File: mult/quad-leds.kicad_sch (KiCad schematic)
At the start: 14 parts, among them U5 LM324

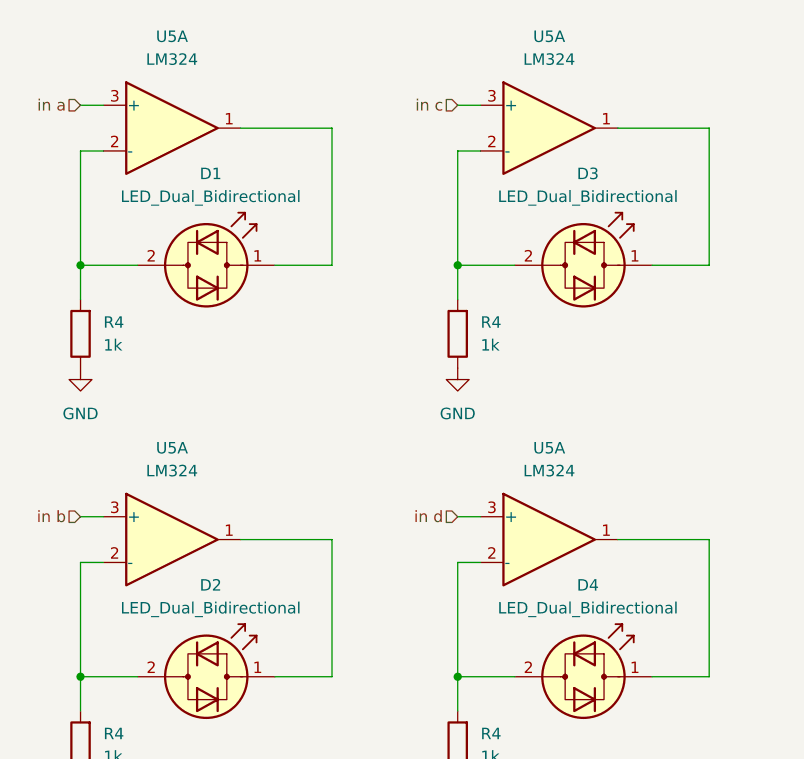
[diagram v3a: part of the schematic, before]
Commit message: mult: Manually assign references, grouped by value
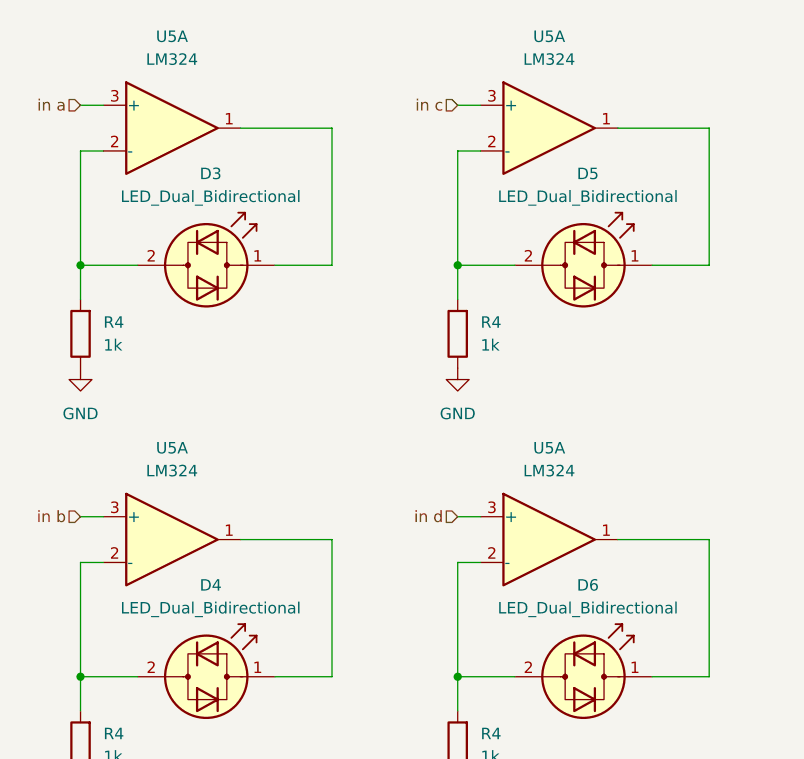
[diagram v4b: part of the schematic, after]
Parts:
- renumbered D1 to D3, D2 to D4, D3 to D5, D4 to D6
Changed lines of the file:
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@@
         )
         (path "/0e98ec4b-b4c7-447c-abd7-a761177a7f67/41fcec89-2c3a-419b-9d1d-2962d3c6916c"
-          (reference "C10") (unit 1)
+          (reference "C12") (unit 1)
         )
       )
@@
   (symbol (lib_id "Device:LED_Dual_Bidirectional") (at 135.89 148.59 0) (unit 1)
     (in_bom yes) (on_board yes) (dnp no) (fields_autoplaced)
-    (property "Reference" "D4" (at 136.3853 138.43 0)
+    (property "Reference" "D6" (at 136.3853 138.43 0)
       (effects (font (size 1.27 1.27)))
     )
@@
       (project "mult"
         (path "/0e98ec4b-b4c7-447c-abd7-a761177a7f67/41fcec89-2c3a-419b-9d1d-2962d3c6916c"
-          (reference "D4") (unit 1)
+          (reference "D6") (unit 1)
         )
       )
@@
   (symbol (lib_id "Device:LED_Dual_Bidirectional") (at 135.89 102.87 0) (unit 1)
     (in_bom yes) (on_board yes) (dnp no) (fields_autoplaced)
-    (property "Reference" "D3" (at 136.3853 92.71 0)
+    (property "Reference" "D5" (at 136.3853 92.71 0)
       (effects (font (size 1.27 1.27)))
     )
@@
       (project "mult"
         (path "/0e98ec4b-b4c7-447c-abd7-a761177a7f67/41fcec89-2c3a-419b-9d1d-2962d3c6916c"
-          (reference "D3") (unit 1)
+          (reference "D5") (unit 1)
         )
       )
@@
   (symbol (lib_id "Device:LED_Dual_Bidirectional") (at 93.98 102.87 0) (unit 1)
     (in_bom yes) (on_board yes) (dnp no) (fields_autoplaced)
-    (property "Reference" "D1" (at 94.4753 92.71 0)
+    (property "Reference" "D3" (at 94.4753 92.71 0)
       (effects (font (size 1.27 1.27)))
     )
@@
       (project "mult"
         (path "/0e98ec4b-b4c7-447c-abd7-a761177a7f67/41fcec89-2c3a-419b-9d1d-2962d3c6916c"
-          (reference "D1") (unit 1)
+          (reference "D3") (unit 1)
         )
       )
@@
   (symbol (lib_id "Device:LED_Dual_Bidirectional") (at 93.98 148.59 0) (unit 1)
     (in_bom yes) (on_board yes) (dnp no) (fields_autoplaced)
-    (property "Reference" "D2" (at 94.4753 138.43 0)
+    (property "Reference" "D4" (at 94.4753 138.43 0)
       (effects (font (size 1.27 1.27)))
     )
@@
       (project "mult"
         (path "/0e98ec4b-b4c7-447c-abd7-a761177a7f67/41fcec89-2c3a-419b-9d1d-2962d3c6916c"
-          (reference "D2") (unit 1)
+          (reference "D4") (unit 1)
         )
       )
@@
         )
         (path "/0e98ec4b-b4c7-447c-abd7-a761177a7f67/41fcec89-2c3a-419b-9d1d-2962d3c6916c"
-          (reference "C9") (unit 1)
-        )
-      )
+          (reference "C11") (unit 1)
+        )
+      )

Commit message: mult: Assign footprints
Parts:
- C1, C2: footprint (none) -> Capacitor_SMD:C_0805_2012Metric
- D3, D4, D5, D6: footprint (none) -> LED_THT:LED_D3.0mm
- R4: footprint (none) -> Resistor_SMD:R_0805_2012Metric
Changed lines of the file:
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@@
       (effects (font (size 1.27 1.27)) (justify right))
     )
-    (property "Footprint" "" (at 81.788 156.21 90)
+    (property "Footprint" "Resistor_SMD:R_0805_2012Metric" (at 81.788 156.21 90)
       (effects (font (size 1.27 1.27)) hide)
     )
@@
       (effects (font (size 1.27 1.27)))
     )
-    (property "Footprint" "" (at 101.6 56.1848 0)
+    (property "Footprint" "Capacitor_SMD:C_0805_2012Metric" (at 101.6 56.1848 0)
       (effects (font (size 1.27 1.27)) hide)
     )
@@
       (effects (font (size 1.27 1.27)))
     )
-    (property "Footprint" "" (at 135.89 148.59 0)
+    (property "Footprint" "LED_THT:LED_D3.0mm" (at 135.89 148.59 0)
       (effects (font (size 1.27 1.27)) hide)
     )
@@
       (effects (font (size 1.27 1.27)) (justify right))
     )
-    (property "Footprint" "" (at 81.788 110.49 90)
+    (property "Footprint" "Resistor_SMD:R_0805_2012Metric" (at 81.788 110.49 90)
       (effects (font (size 1.27 1.27)) hide)
     )
@@
       (effects (font (size 1.27 1.27)))
     )
-    (property "Footprint" "" (at 135.89 102.87 0)
+    (property "Footprint" "LED_THT:LED_D3.0mm" (at 135.89 102.87 0)
       (effects (font (size 1.27 1.27)) hide)
     )
@@
       (effects (font (size 1.27 1.27)) (justify right))
     )
-    (property "Footprint" "" (at 123.698 156.21 90)
+    (property "Footprint" "Resistor_SMD:R_0805_2012Metric" (at 123.698 156.21 90)
       (effects (font (size 1.27 1.27)) hide)
     )
@@
       (effects (font (size 1.27 1.27)))
     )
-    (property "Footprint" "" (at 93.98 102.87 0)
+    (property "Footprint" "LED_THT:LED_D3.0mm" (at 93.98 102.87 0)
       (effects (font (size 1.27 1.27)) hide)
     )
@@
       (effects (font (size 1.27 1.27)) (justify right))
     )
-    (property "Footprint" "" (at 123.698 110.49 90)
+    (property "Footprint" "Resistor_SMD:R_0805_2012Metric" (at 123.698 110.49 90)
       (effects (font (size 1.27 1.27)) hide)
     )
@@
       (effects (font (size 1.27 1.27)))
     )
-    (property "Footprint" "" (at 93.98 148.59 0)
+    (property "Footprint" "LED_THT:LED_D3.0mm" (at 93.98 148.59 0)
       (effects (font (size 1.27 1.27)) hide)
     )
@@
       (effects (font (size 1.27 1.27)))
     )
-    (property "Footprint" "" (at 101.6 40.9448 0)
-      (effects (font (size 1.27 1.27)) hide)
-    )
+    (property "Footprint" "Capacitor_SMD:C_0805_2012Metric" (at 101.6 40.9448 0)
+      (effects (font (size 1.27 1.27)) hide)
+    )

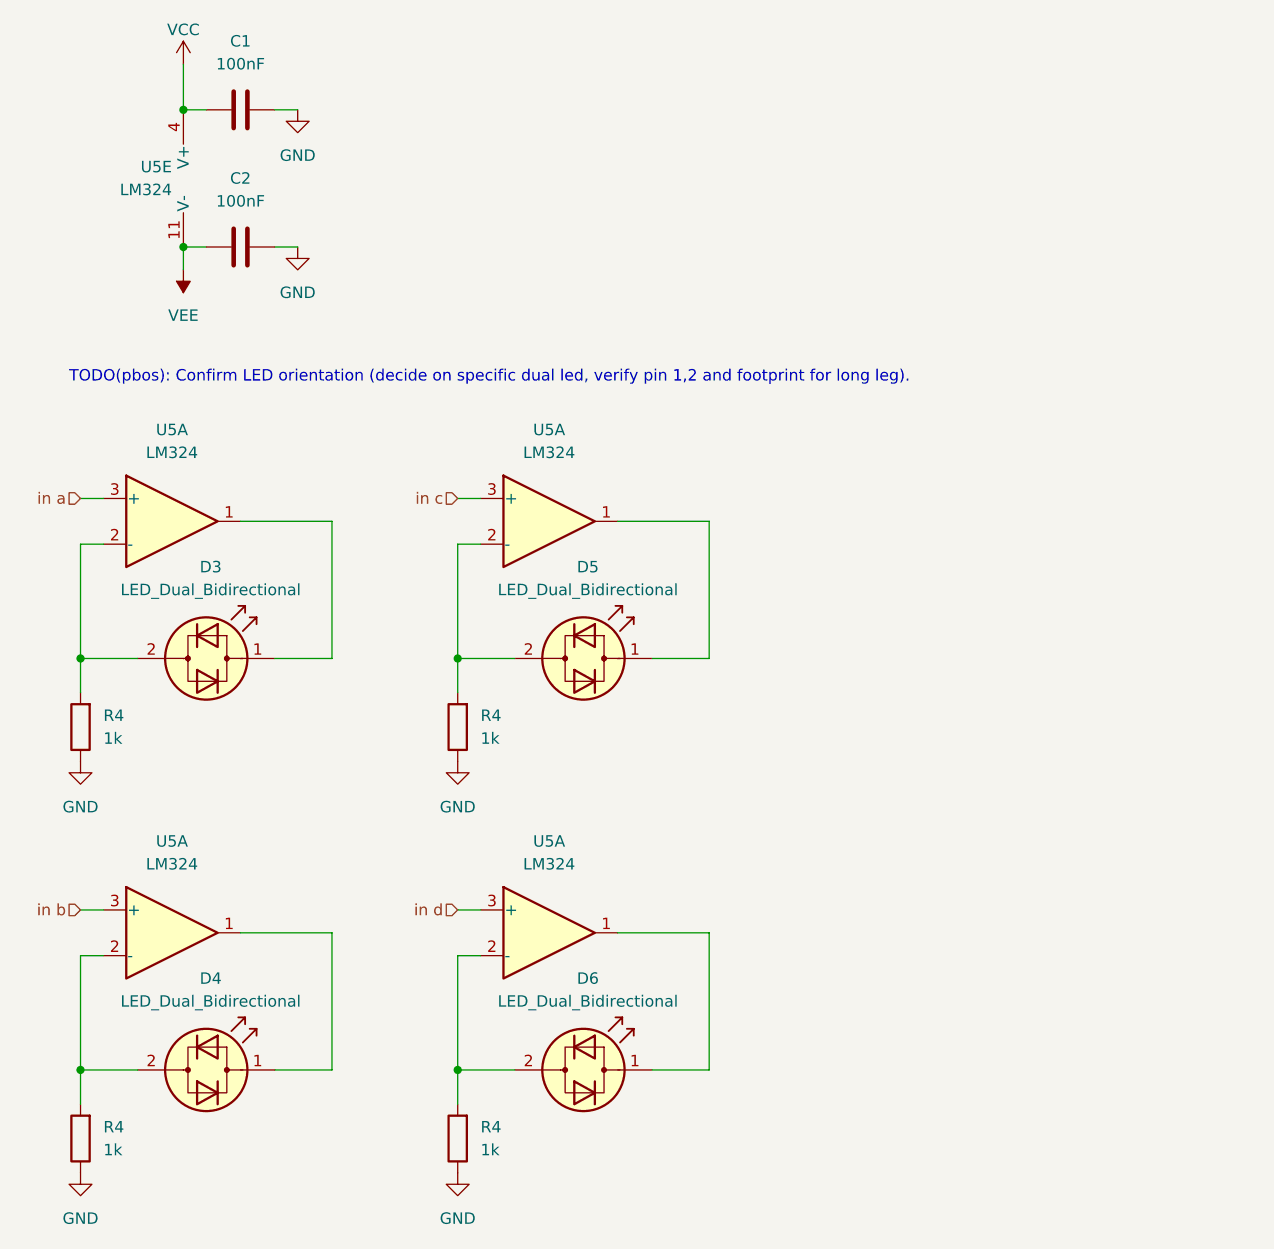
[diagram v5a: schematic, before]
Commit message: mult: Misc partial progress
At least since last commit:

* New LEDs (no dual unit)
* Jack placement, share sleeve pin
* Board fit within 20x108mm
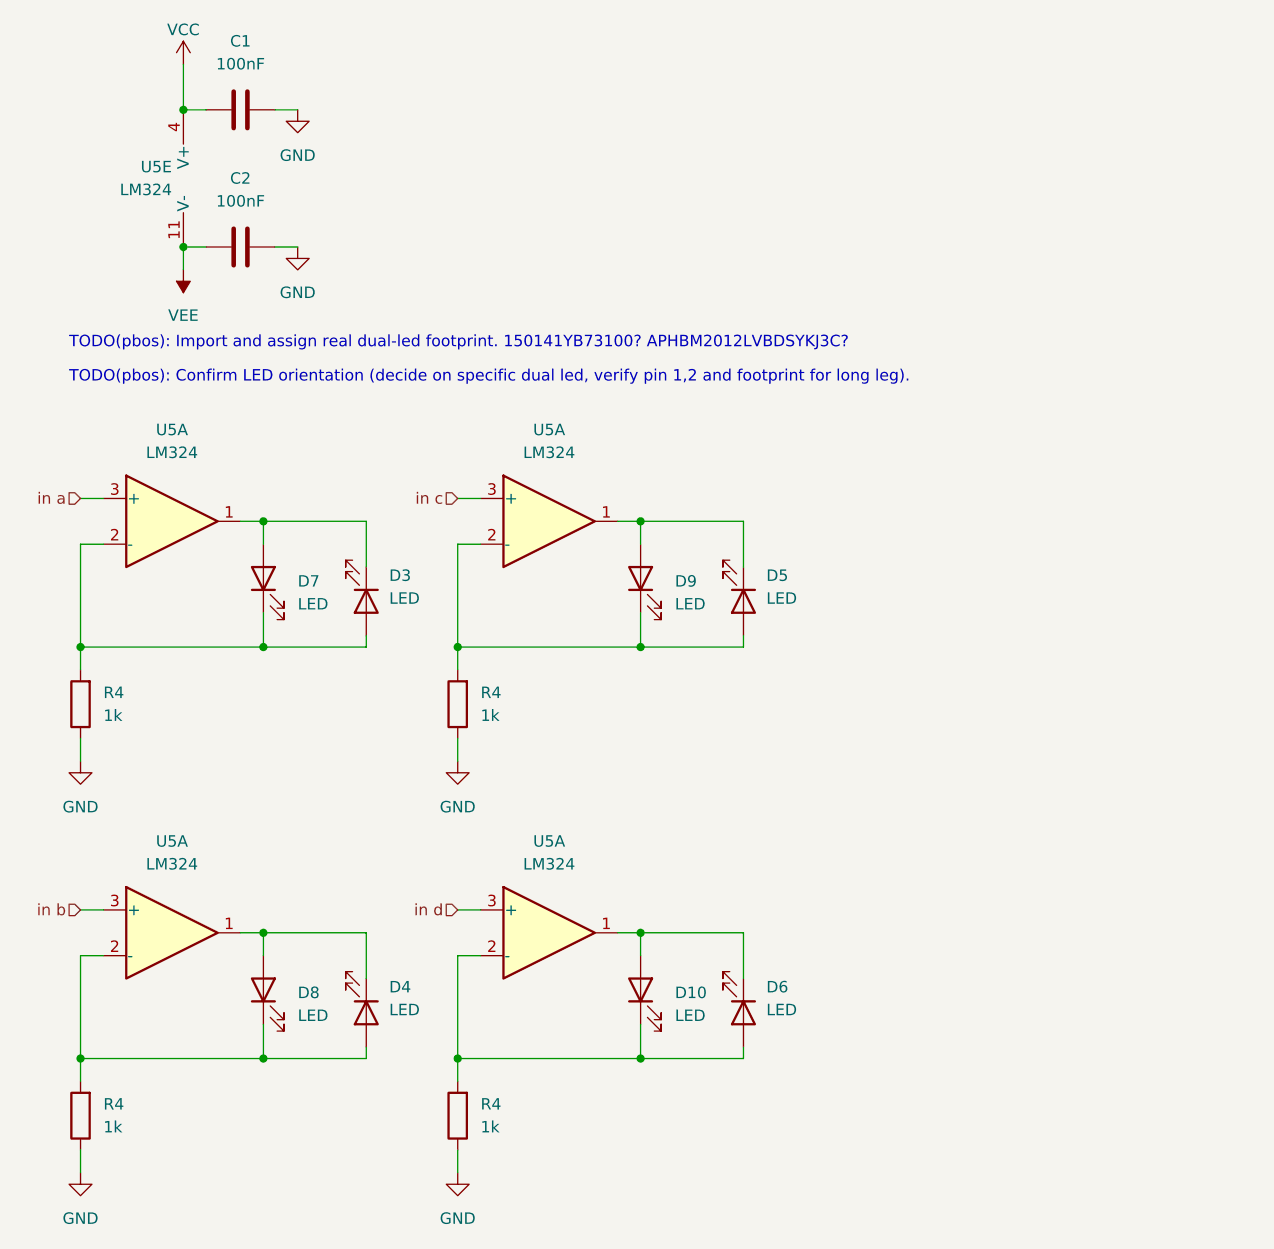
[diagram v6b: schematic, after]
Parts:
- removed D3, D4, D5, D6: LED_Dual_Bidirectional, LED_THT:LED_D3.0mm, symbol Device:LED_Dual_Bidirectional
- removed R4 (x3): 1k, Resistor_SMD:R_0805_2012Metric, symbol Device:R
- added D10, D3, D4, D5, D6, D7, D8, D9: LED, LED_SMD:LED_0805_2012Metric_Pad1.15x1.40mm_HandSolder, symbol Device:LED
- added R4 (x3): 1k, Resistor_SMD:R_0805_2012Metric_Pad1.20x1.40mm_HandSolder, symbol Device:R
- C1, C2: footprint Capacitor_SMD:C_0805_2012Metric -> Capacitor_SMD:C_0805_2012Metric_Pad1.18x1.45mm_HandSolder
- R4: footprint Resistor_SMD:R_0805_2012Metric -> Resistor_SMD:R_0805_2012Metric_Pad1.20x1.40mm_HandSolder
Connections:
- net GND: now also R4.1, R4.1, R4.1
- net at U5.1: now also D10.2 (A), D6.1 (K)
- net at U5.2 (-): now also D10.1 (K), D6.2 (A), R4.2
- net at U5.2 (-): now also D4.2 (A), D8.1 (K), R4.2
- net at R4.2, U5.2 (-): now also D3.2 (A), D7.1 (K)
- net at U5.1: now also D5.1 (K), D9.2 (A)
- net at U5.2 (-): now also D5.2 (A), D9.1 (K), R4.2
- net at U5.1: now also D3.1 (K), D7.2 (A)
- net at U5.1: now also D4.1 (K), D8.2 (A)
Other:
- note added: "TODO(pbos): Import and assign real dual-led footprint. 150141YB73100? APHBM2012LVBDSYKJ3C?"
- moved on the sheet: R4
